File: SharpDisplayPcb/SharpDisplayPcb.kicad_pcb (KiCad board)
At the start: 2 copper layers, 53.2 x 52.4 mm, 2 parts

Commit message: PCB border, start schematic
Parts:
- removed REF**: PinHeader_1x08_P2.54mm_Vertical, Connector_PinHeader_2.54mm:PinHeader_1x08_P2.54mm_Vertical
- added J1: Conn_01x08_Female, Connector_PinHeader_2.54mm:PinHeader_1x08_P2.54mm_Vertical, F.Cu at (100.0, 103.9)
- added M3: MH3, MountingHole:MountingHole_3mm_Pad, F.Cu at (124.6, 103.4)
- added M3: MH3, MountingHole:MountingHole_3mm_Pad, F.Cu at (90.6, 103.4)
- added M3: MH3, MountingHole:MountingHole_3mm_Pad, F.Cu at (90.6, 70.4)
- M3: renamed from REF**; value MountingHole_3mm_Pad -> MH3
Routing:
- added copper zone on B.Cu, net GND
- added copper zone on F.Cu, net GND
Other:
- board size 53.2 x 52.4 mm -> 40 x 39 mm

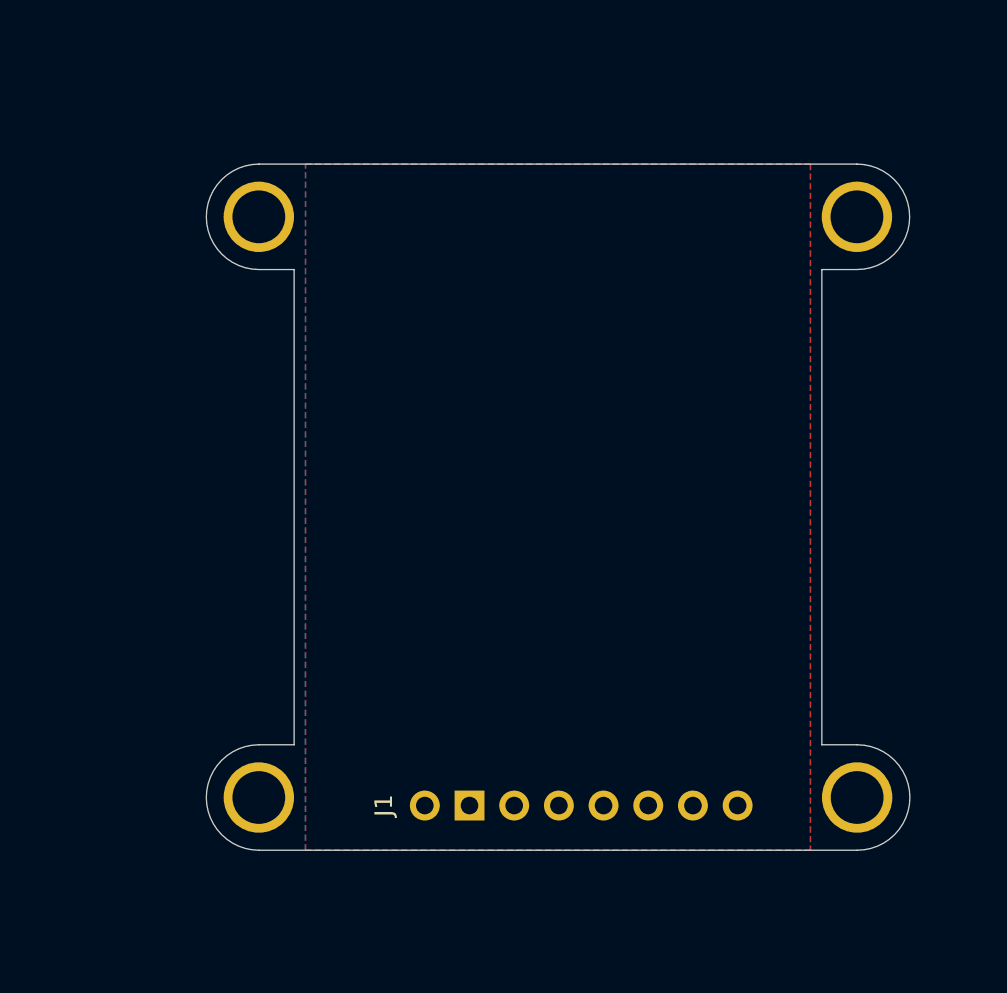
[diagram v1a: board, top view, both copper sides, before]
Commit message: Completed schematics, initial PCB layout
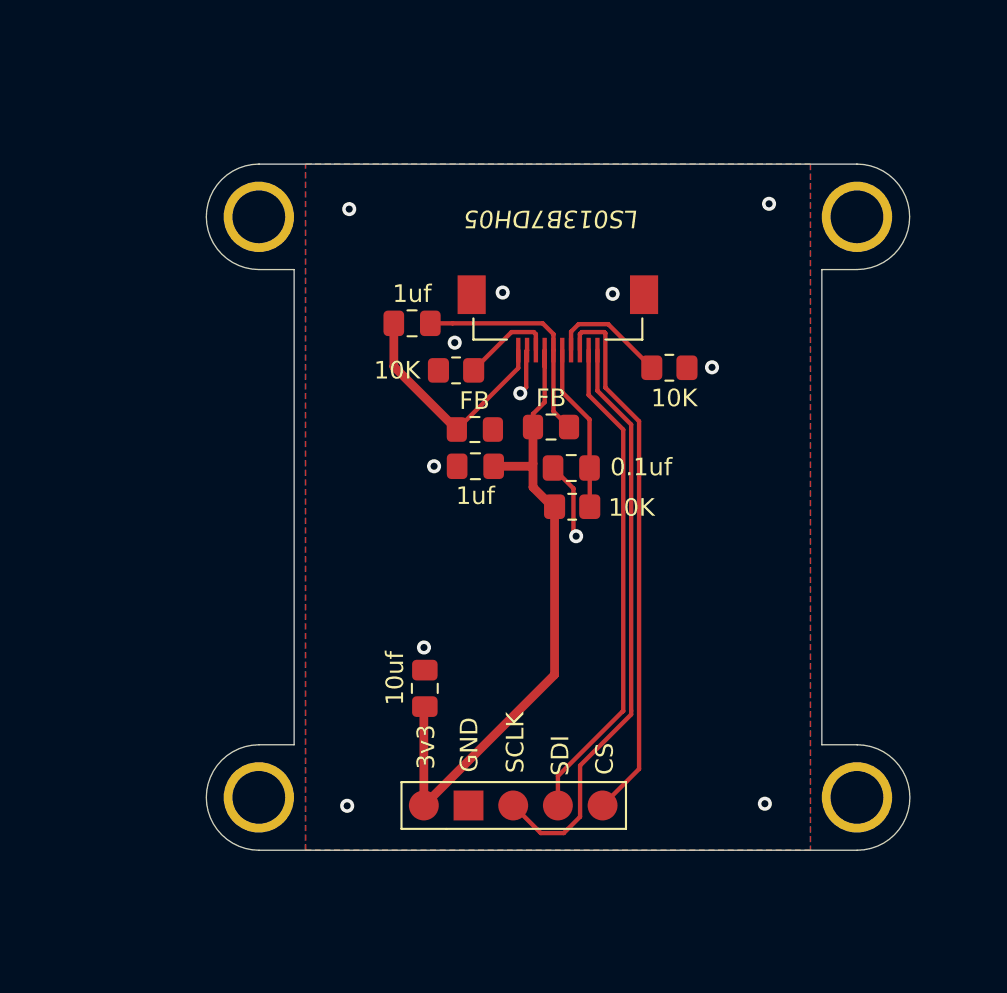
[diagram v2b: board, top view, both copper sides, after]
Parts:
- added C1: 10uf, Capacitor_SMD:C_0805_2012Metric_Pad1.18x1.45mm_HandSolder, F.Cu at (100.0, 97.2)
- added C2: 0.1uf, Capacitor_SMD:C_0805_2012Metric_Pad1.18x1.45mm_HandSolder, F.Cu at (108.3, 84.7)
- added C3: 1uf, Capacitor_SMD:C_0805_2012Metric_Pad1.18x1.45mm_HandSolder, F.Cu at (102.9, 84.6)
- added C4: 1uf, Capacitor_SMD:C_0805_2012Metric_Pad1.18x1.45mm_HandSolder, F.Cu at (99.3, 76.5)
- added FB1: FB, Inductor_SMD:L_0805_2012Metric_Pad1.15x1.40mm_HandSolder, F.Cu at (102.9, 82.5)
- added FB2: FB, Inductor_SMD:L_0805_2012Metric_Pad1.15x1.40mm_HandSolder, F.Cu at (107.2, 82.3)
- added IC1: LS013B7DH05, SharpDisplay:FPC_10PIN_52892-1033, F.Cu at (107.6, 78.0)
- added R1: 10K, Resistor_SMD:R_0805_2012Metric_Pad1.20x1.40mm_HandSolder, F.Cu at (113.9, 79.0)
- added R2: 10K, Resistor_SMD:R_0805_2012Metric_Pad1.20x1.40mm_HandSolder, F.Cu at (101.8, 79.1)
- added R3: 10K, Resistor_SMD:R_0805_2012Metric_Pad1.20x1.40mm_HandSolder, F.Cu at (108.4, 86.9)
- J1: value Conn_01x08_Female -> SMD Connector; footprint Connector_PinHeader_2.54mm:PinHeader_1x08_P2.54mm_Vertical -> Connector_PinHeader_2.54mm:PinHeader_1x05_P2.54mm_Vertical
- moved J1 0.06 mm to (100.0, 103.9)
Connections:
- J1 pad 1: Net-(J1-Pad1) -> +3V3
- J1 pad 3: Net-(J1-Pad3) -> SCLK
- J1 pad 4: Net-(J1-Pad4) -> SDI
- J1 pad 5: Net-(J1-Pad5) -> CS
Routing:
- net +3V3: track 0.00 -> 38.7 mm
- net SCLK: track 0.00 -> 33.4 mm
- net CS: track 0.00 -> 30.9 mm
- net SDI: track 0.00 -> 28.3 mm
- net GNDA: track 0.00 -> 13.5 mm
- net +3.3VA: track 0.00 -> 12.9 mm
- net Net-(C2-Pad2): track 0.00 -> 9.55 mm
- net GND: track 0.00 -> 6.99 mm, vias 0 -> 12
- net Net-(IC1-PadEXTCOMIN): track 0.00 -> 6.84 mm
- net Net-(IC1-PadEXTMODE): track 0.00 -> 5.41 mm
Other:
- board text added: "3v3"
- board text added: "CS"
- board text added: "GND"
- board text added: "SCLK"
- board text added: "SDI"

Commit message: Add DISP jumper, to disable pull-up resistor
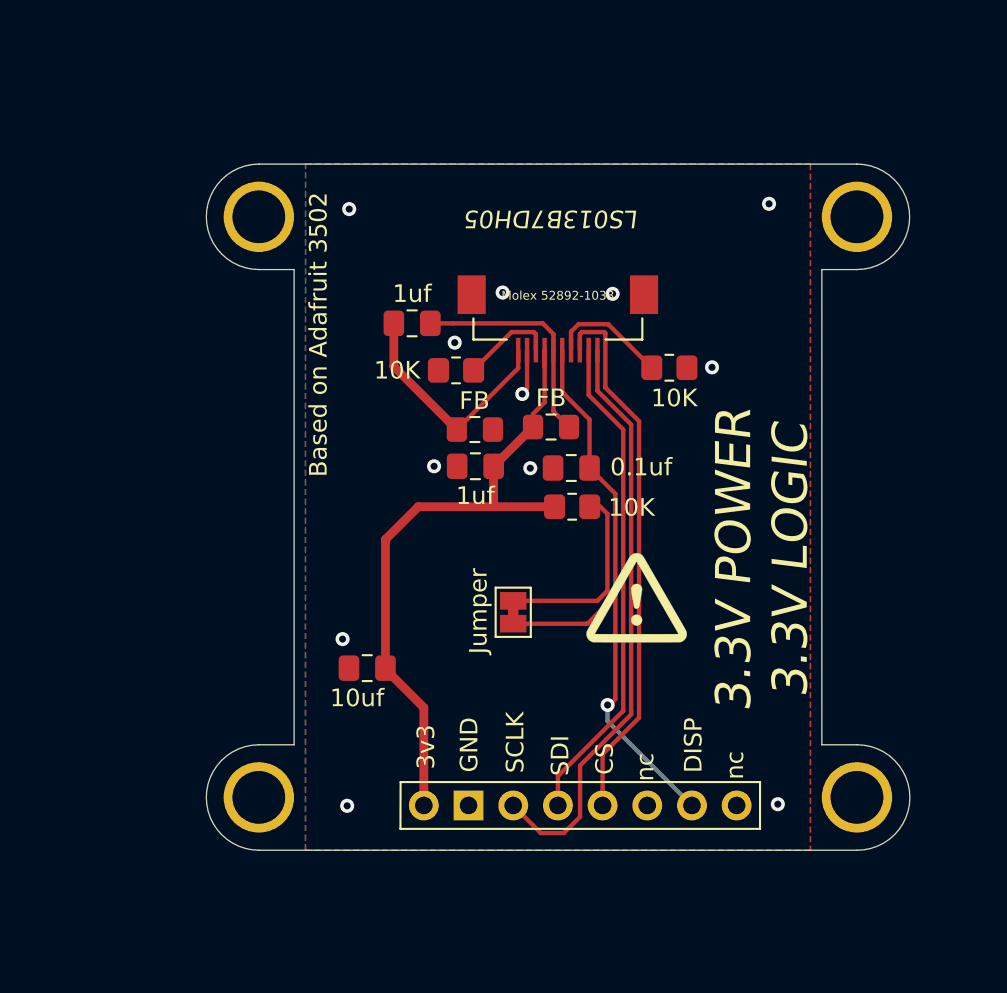
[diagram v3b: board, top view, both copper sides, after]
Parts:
- added G***: LOGO, SharpDisplay:warning, F.Cu at (112.1, 92.0)
- added JP1: Jumper, Jumper:SolderJumper-2_P1.3mm_Bridged_Pad1.0x1.5mm, F.Cu at (105.0, 92.9)
- J1: value SMD Connector -> Conn_01x08_Female; footprint Connector_PinHeader_2.54mm:PinHeader_1x05_P2.54mm_Vertical -> Connector_PinHeader_2.54mm:PinHeader_1x08_P2.54mm_Vertical
- moved C1 3.47 mm to (96.8, 96.0), turned to 180 degrees
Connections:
- C2 pad 2: Net-(C2-Pad2) -> BLANK
- IC1 pad DISP: Net-(C2-Pad2) -> BLANK
- R3 pad 2: Net-(C2-Pad2) -> Net-(JP1-Pad2)
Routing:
- net BLANK: track 0.00 -> 36.4 mm, vias 0 -> 1
- net Net-(JP1-Pad2): track 0.00 -> 11.1 mm
- net Net-(C2-Pad2): track 9.55 -> 0.00 mm
- net GND: track 6.99 -> 2.62 mm
- net +3V3: track 38.7 -> 37.7 mm
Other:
- board text added: "3.3V POWER 3.3V LOGIC"
- board text added: "Based on Adafruit 3502"
- board text added: "DISP"
- board text added: "nc"

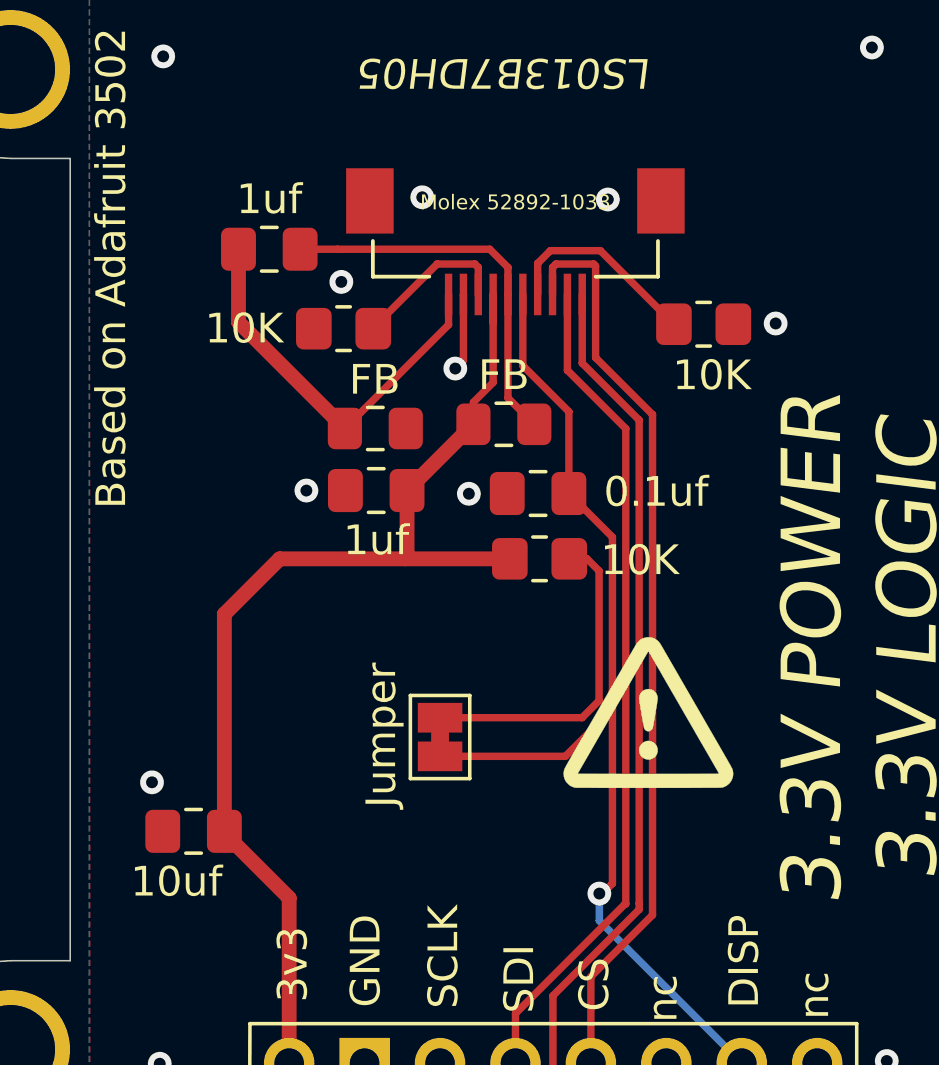
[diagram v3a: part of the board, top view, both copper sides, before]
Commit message: Better routing for 3v3 bypass capacitor
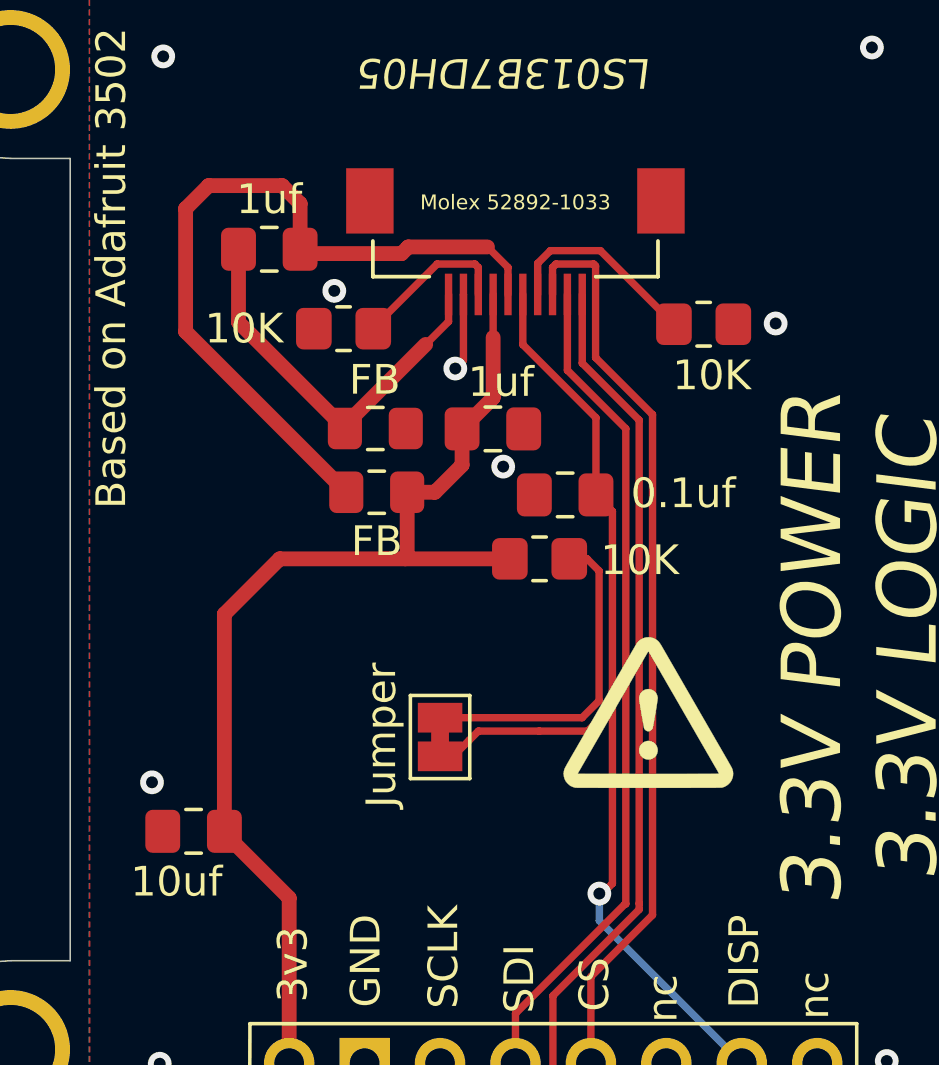
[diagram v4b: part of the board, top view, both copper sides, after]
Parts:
- moved FB2 4.85 mm to (102.9, 84.6), turned to 0 degrees
- moved C3 4.44 mm to (106.8, 82.5), turned to 180 degrees
- moved C2 0.91 mm to (109.3, 84.7)
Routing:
- net +3.3VA: track 12.9 -> 26.1 mm
- net GND: vias 12 -> 9

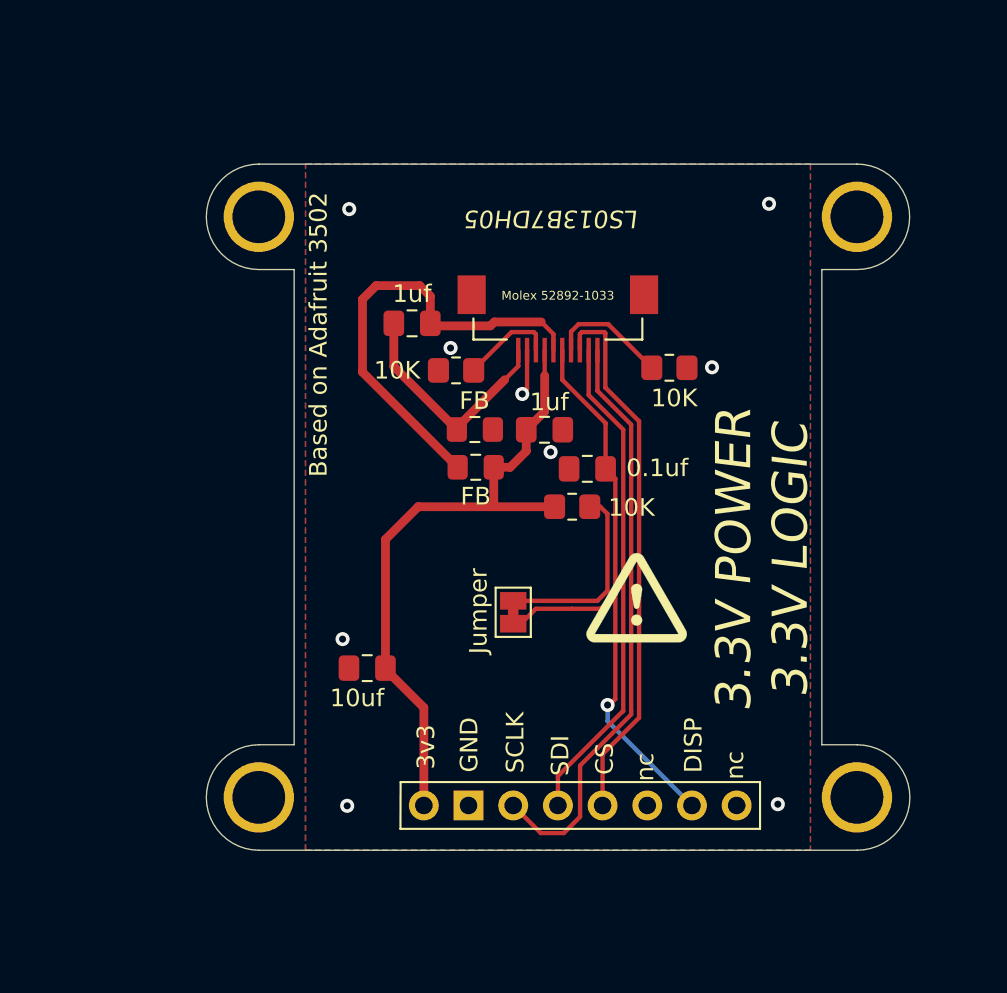
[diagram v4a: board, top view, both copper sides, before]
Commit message: Remove pull-down resistors, adjust layout
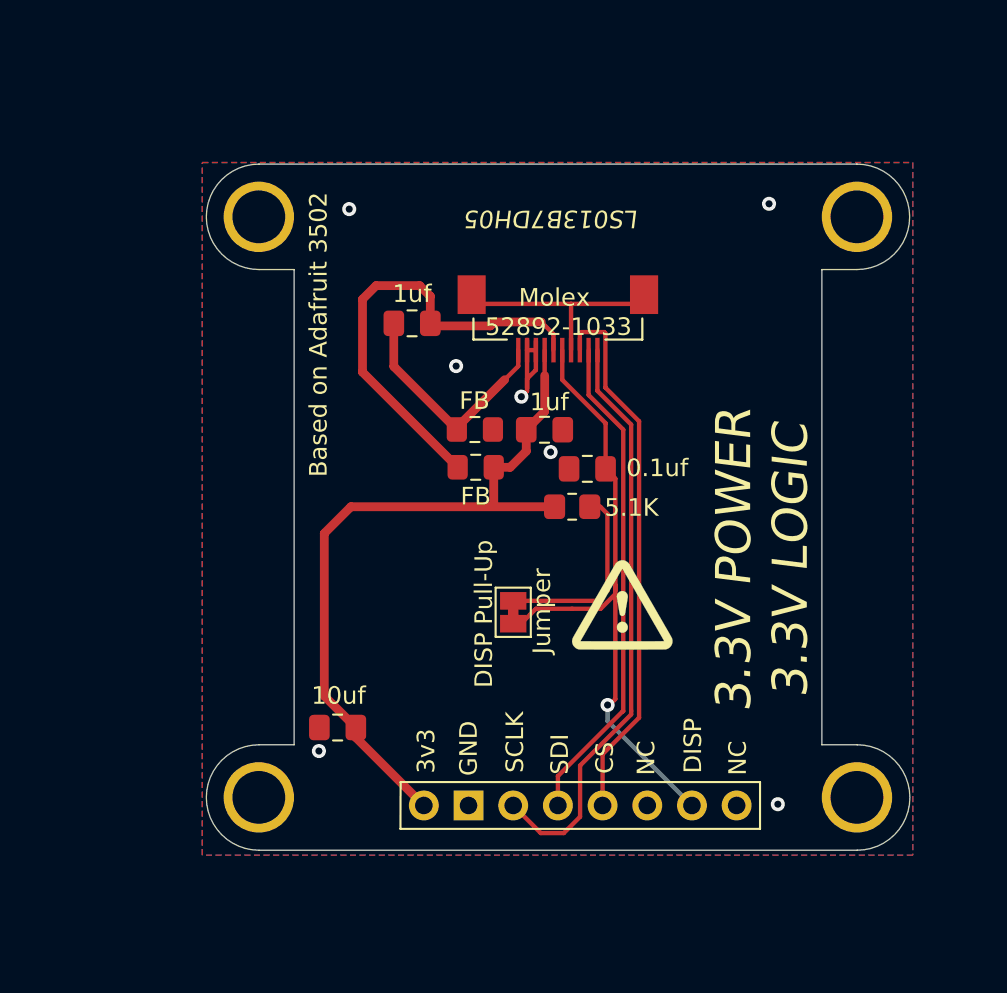
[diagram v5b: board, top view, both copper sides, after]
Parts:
- removed the R1 at (113.9, 79.0)
- removed R2: 10K, Resistor_SMD:R_0805_2012Metric_Pad1.20x1.40mm_HandSolder
- R1: renamed from R3; value 10K -> 5.1K
- moved C1 3.77 mm to (95.1, 99.4)
- moved G*** 0.91 mm to (111.3, 92.5)
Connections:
- IC1 pad EXTCOMIN: Net-(IC1-PadEXTCOMIN) -> GND
- IC1 pad EXTMODE: Net-(IC1-PadEXTMODE) -> GND
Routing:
- net GND: track 2.62 -> 19.6 mm, vias 9 -> 7
- net Net-(IC1-PadEXTCOMIN): track 6.84 -> 0.00 mm
- net Net-(IC1-PadEXTMODE): track 5.41 -> 0.00 mm
- net +3V3: track 37.3 -> 42.3 mm
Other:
- board text added: "DISP Pull-Up"
- board text added: "Molex"
- board text added: "NC"
- board text removed: "nc"

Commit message: Replace ZIF part, move components out of ZIF footprint
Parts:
- removed IC1: LS013B7DH05, SharpDisplay:FPC_10PIN_52892-1033
- added J2: 5052781033, SharpDisplay:5052781033, F.Cu at (107.6, 75.7)
- moved FB2 5.56 mm to (97.4, 84.1)
- moved FB1 5.56 mm to (97.4, 81.8)
- moved C3 5.12 mm to (101.7, 83.0), turned to 270 degrees
- moved C4 2.13 mm to (97.2, 76.6), turned to 0 degrees
- moved C1 1.67 mm to (95.6, 97.9), turned to 0 degrees
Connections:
- C4 pad 1: +3.3VA -> GNDA
- C4 pad 2: GNDA -> +3.3VA
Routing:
- net +3V3: track 42.3 -> 49.5 mm
- net +3.3VA: track 26.1 -> 22.5 mm
- net GND: track 19.6 -> 17.9 mm, vias 7 -> 4
- net GNDA: track 13.5 -> 15.1 mm
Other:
- rule pad_to_mask_clearance: 0 -> 0.05
- board text added: "Pull-Up"
- board text removed: "DISP Pull-Up"
